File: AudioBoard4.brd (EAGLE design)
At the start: 165.2 x 136.7 mm, 294 parts, among them IC1 TL084D, IC10 TL084D, IC11 TL074D, IC13 SSM2164P, IC14 TL071D, IC15 TL084D, IC16 TL071D, IC17 TL084D, IC18 SSM2164P, IC19 TL071D, IC2 TL074D, IC20 TL084D, IC21 TL071D, IC22 TL084D, IC23 TL072D, IC24 LT1054, IC25 7905, IC26 7805, IC4 TL084D, IC5 TL074D, IC7 TL084D, IC8 TL074D

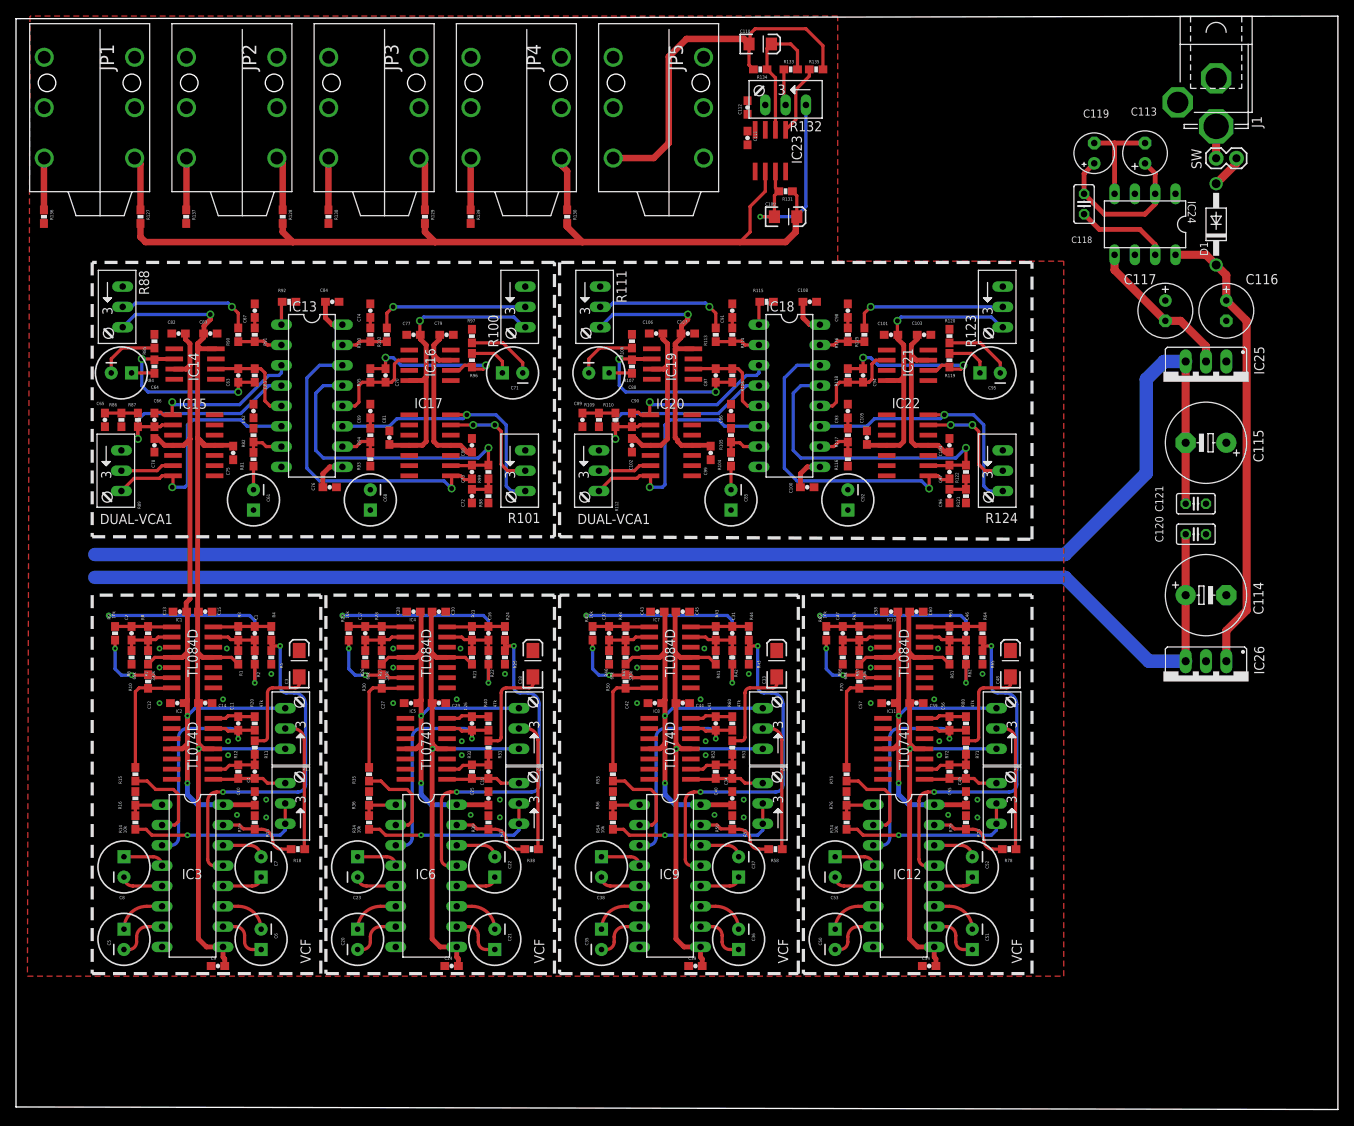
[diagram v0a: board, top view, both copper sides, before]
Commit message: Update eagle files to contain powerdown signal.
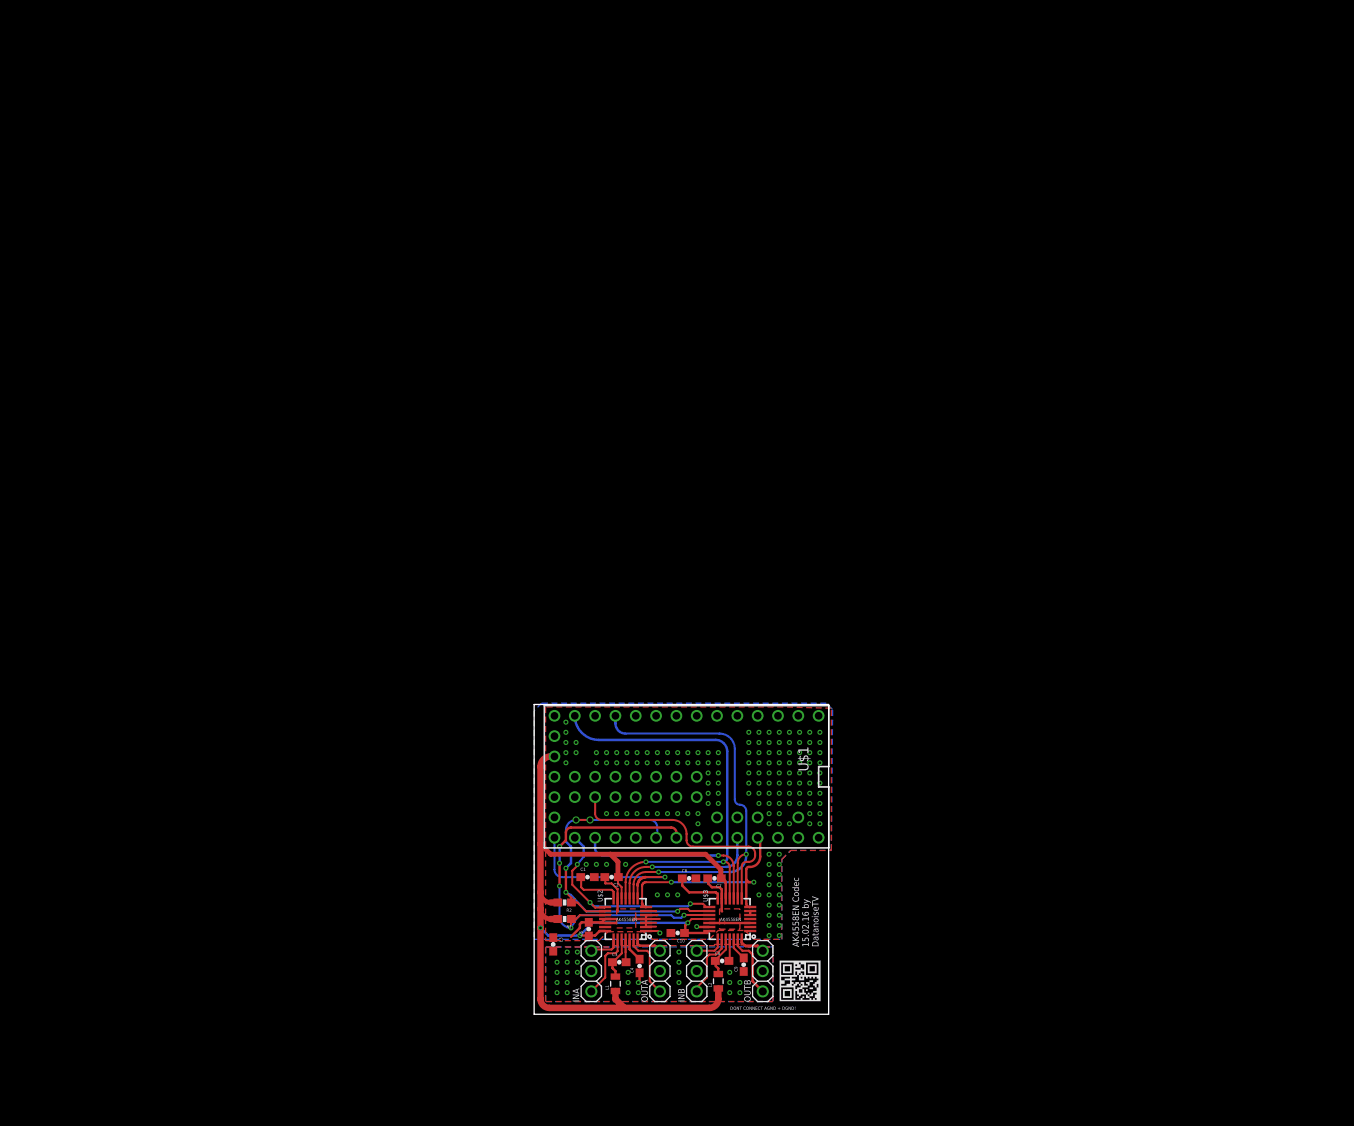
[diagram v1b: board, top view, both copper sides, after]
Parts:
- removed C100, C101, C102, C103, C104, C105, C106, C107, C108, C111, C112, C75, C76, C77, C78, C79, C80, C81, C82, C83, C84, C99: 100n, SparkFun-Capacitors:0603-CAP
- removed C109: 100p, SparkFun-Capacitors:EIA3216
- removed C11, C26, C41, C56: 100pF, SparkFun-Capacitors:0603-CAP
- removed C110: 18p, SparkFun-Capacitors:EIA3216
- removed C113: 100u, rcl:E2,5-6
- removed C114, C115: 220u, rcl:E5-10,5
- removed C116, C117: 100u, rcl:E2,5-7
- removed C118: 10p, rcl:C025-025X050
- removed C119: 10u, rcl:E2,5-5
- removed C12, C13, C14, C15, C24, C25, C27, C28, C29, C30, C39, C40, C42, C43, C44, C45, C54, C55, C57, C58, C59, C60: 100nF, SparkFun-Capacitors:0603-CAP
- removed C120, C121: 100n, rcl:C025-025X050
- removed C16, C17, C31, C32, C46, C47: 22nF, SparkFun-Capacitors:0603-CAP
- removed C18, C33, C48: (no value), SparkFun-Capacitors:EIA3216-KIT
- removed C19, C34, C49: 1.5nF, SparkFun-Capacitors:0603-CAP
- removed C20, C21, C22, C35, C36, C37, C50, C51, C52: 10n, SparkFun-Passives:CPOL-RADIAL-100UF-25V
- removed C23, C38, C53: 820p, SparkFun-Capacitors:CPOL-RADIAL-100UF-25V
- removed C61, C68, C85, C92: 1uF, SparkFun-Capacitors:CPOL-RADIAL-100UF-25V
- removed C62, C67, C69, C74, C86, C91, C93, C98: 560p, SparkFun-Capacitors:0603-CAP
- removed C63, C66, C70, C73, C87, C90, C94, C97: 100p, SparkFun-Capacitors:0603-CAP
- removed C64, C71, C88, C95: 10uF, SparkFun-Capacitors:CPOL-RADIAL-100UF-25V
- removed C65, C72, C89, C96: 33nF, SparkFun-Capacitors:0603-CAP
- removed D1: 1N4001, diode:DO41-10
- removed IC1, IC10, IC15, IC17, IC20, IC22, IC4, IC7: TL084D, linear:SO14
- removed IC11, IC2, IC5, IC8: TL074D, linear:SO14
- removed IC12, IC3, IC6, IC9: (no value), ic-package:DIL16
- removed IC13, IC18: SSM2164P, ssm2164:DIL16
- removed IC14, IC16, IC19, IC21: TL071D, linear:SO08
- removed IC23: TL072D, linear:SO08
- removed IC24: LT1054, ic-package:DIL08
- removed IC25: 7905, v-reg:79XXS
- removed IC26: 7805, v-reg:78XXS
- removed J1: (no value), con-jack2:SPC4078_BIG_HOLES
- removed JP1, JP2, JP3, JP4, JP5: AUDIO-JACK4-.25-HORIZ-TRS, SparkFun-Connectors:AUDIO-JACK-.25-INCH-HORIZ-PTH
- removed R10, R108, R109, R110, R12, R120, R121, R122, R14, R24, R29, R30, R32, R34, R4, R44, R49, R50, R52, R54, R64, R69, R70, R72, R74, R85, R86, R87, R9, R97, R98, R99: 10k, SparkFun-Passives:0603-RES
- removed R100, R111, R123, R88: 100k, pot:RJ9W
- removed R101, R112, R124, R89: 50k, pot:RJ9W
- removed R102, R113, R125, R133, R134, R21, R41, R61, R90: 100k, SparkFun-Passives:0603-RES
- removed R103, R105, R114, R117, R126, R135, R136, R137, R138, R139, R82, R91, R94: 470, SparkFun-Passives:0603-RES
- removed R104, R116, R22, R42, R62, R81, R93: 33k, SparkFun-Passives:0603-RES
- removed R106, R118, R20, R40, R60, R80, R83, R95: 47k, SparkFun-Passives:0603-RES
- removed R107, R119, R15, R35, R55, R75, R84, R96: 150, SparkFun-Passives:0603-RES
- removed R11, R23, R28, R3, R31, R43, R48, R51, R63, R68, R71, R8: 22k, SparkFun-Passives:0603-RES
- removed R115, R92: 4.7k, SparkFun-Passives:0603-RES
- removed R127, R128, R129, R130: 10K, SparkFun-Passives:0603-RES
- removed R13, R33, R53, R73: INPUT_LVL, pot:RJ9W
- removed R131: RGAIN, SparkFun-Passives:0603-RES
- removed R132: 100K, pot:RJ9W
- removed R16, R19, R36, R39, R56, R59, R76, R79: 220, SparkFun-Passives:0603-RES
- removed R17, R37, R57, R77: OFFS_ADJ, pot:RJ9W
- removed R18, R38, R58, R78: 390k, SparkFun-Passives:0603-RES
- removed R25, R45, R5, R65: 1k, SparkFun-Passives:0603-RES
- removed R26, R46, R6, R66: 68k, SparkFun-Passives:0603-RES
- removed R27, R47, R67, R7: 330k, SparkFun-Passives:0603-RES
- removed SW: (no value), SparkFun:1X02
- added INA, INB, OUTA, OUTB: (no value), adafruit:1X03
- added L1, L2: 10uH, SparkFun-Passives:0805
- added L3: 10uH, SparkFun-Passives:0603
- added U$1: TEENSY_3.0_ALL_PINS_AND_PADS, Teensy_3_Series_Board_v1.0:TEENSY_3.0_ALLPINS
- added U$2, U$3: AK4558EN, AK4558:QFN-28-5MM
- C1, C2: value 22nF -> 100n; device SparkFun-Capacitors:0603-CAP -> SparkFun-Passives:0603-CAP
- C10, C9: value 100nF -> 100n; device SparkFun-Capacitors:0603-CAP -> SparkFun-Passives:0603-CAP
- C3: value (none) -> 100n; device SparkFun-Capacitors:EIA3216-KIT -> SparkFun-Passives:0603-CAP
- C4: value 1.5nF -> 100n; device SparkFun-Capacitors:0603-CAP -> SparkFun-Passives:0603-CAP
- C5, C6, C7: value 10n -> 100n; device SparkFun-Passives:CPOL-RADIAL-100UF-25V -> SparkFun-Passives:0603-CAP
- C8: value 820p -> 100n; device SparkFun-Capacitors:CPOL-RADIAL-100UF-25V -> SparkFun-Passives:0603-CAP
- R1: value 100k -> 1k
- R2: value 33k -> 1k
- moved C8 75.7 mm to (87.6, 18.4), turned to 0 degrees
- moved C2 67.3 mm to (73.8, 28.9), turned to 180 degrees
- moved C9 65.7 mm to (90.3, 17.9), turned to 90 degrees
- moved C5 58.1 mm to (71.0, 22.4)
- moved C7 56.7 mm to (86.7, 28.7), turned to 180 degrees
- moved C10 55.5 mm to (82.1, 21.9), turned to 180 degrees
- moved C3 54.7 mm to (74.8, 18.3), turned to 0 degrees
- moved C6 54.0 mm to (83.5, 28.7), turned to 0 degrees
- moved C4 53.9 mm to (77.3, 17.8), turned to 90 degrees
- moved R1 52.3 mm to (67.9, 23.7), turned to 180 degrees
- moved C1 51.6 mm to (70.8, 28.9), turned to 0 degrees
- moved R2 49.4 mm to (67.9, 25.7), turned to 180 degrees
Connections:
- removed net N$100: C63.2, IC13.5, IC14.2, R83.1
- removed net N$101: C63.1, IC14.6, R83.2, R84.1
- removed net N$102: C64.1, R84.2
- removed net N$103: C65.2, R86.2, R87.1
- removed net N$104: C66.2, IC13.4, IC15.2, R87.2
- removed net N$105: C66.1, IC13.3, IC15.1, IC15.5
- removed net N$106: IC13.2, R90.1, R91.2
- removed net N$107: R88.S, R90.2
- removed net N$108: C67.2, R91.1
- removed net N$109: IC13.6, IC15.7, R89.A
- removed net N$110: IC15.6, R89.S
- removed net N$111: IC13.1, R92.2
- removed net N$112: C68.2, R93.1
- removed net N$113: IC13.10, R93.2, R94.2
- removed net N$114: C69.2, R94.1
- removed net N$115: C70.2, IC13.12, IC16.2, R95.1
- removed net N$116: C70.1, IC16.6, R95.2, R96.1
- removed net N$117: C71.1, R96.2
- removed net N$118: IC13.11, IC17.7, R101.A
- removed net N$119: C72.2, R98.2, R99.1
- removed net N$120: C73.2, IC13.13, IC17.2, R99.2
- removed net N$121: C73.1, IC13.14, IC17.1, IC17.5
- removed net N$122: IC13.15, R102.1, R103.2
- removed net N$123: R100.S, R102.2
- removed net N$124: C74.2, R103.1
- removed net N$125: IC17.6, R101.S
- removed net N$126: C85.2, R104.1
- removed net N$127: IC18.7, R104.2, R105.2
- removed net N$128: C86.2, R105.1
- removed net N$129: C87.2, IC18.5, IC19.2, R106.1
- removed net N$130: C87.1, IC19.6, R106.2, R107.1
- removed net N$131: C88.1, R107.2
- removed net N$132: C89.2, R109.2, R110.1
- removed net N$133: C90.2, IC18.4, IC20.2, R110.2
- removed net N$134: C90.1, IC18.3, IC20.1, IC20.5
- removed net N$135: IC18.2, R113.1, R114.2
- removed net N$136: R111.S, R113.2
- removed net N$137: C91.2, R114.1
- removed net N$138: IC18.6, IC20.7, R112.A
- removed net N$139: IC20.6, R112.S
- removed net N$140: IC18.1, R115.2
- removed net N$141: C92.2, R116.1
- removed net N$142: IC18.10, R116.2, R117.2
- removed net N$143: C93.2, R117.1
- removed net N$144: C94.2, IC18.12, IC21.2, R118.1
- removed net N$145: C94.1, IC21.6, R118.2, R119.1
- removed net N$146: C95.1, R119.2
- removed net N$147: IC18.11, IC22.7, R124.A
- removed net N$148: C96.2, R121.2, R122.1
- removed net N$149: C97.2, IC18.13, IC22.2, R122.2
- removed net N$150: C97.1, IC18.14, IC22.1, IC22.5
- removed net N$151: IC18.15, R125.1, R126.2
- removed net N$152: R123.S, R125.2
- removed net N$153: C98.2, R126.1
- removed net N$154: IC22.6, R124.S
- removed net N$155: C109.A, IC23.6, R127.2, R128.2, R129.2, R130.2, R131.1
- removed net N$156: C109.C, IC23.7, R131.2, R132.E
- removed net N$157: R132.S, R133.1
- removed net N$158: C110.A, IC23.2, R133.2, R134.1
- removed net N$159: C110.C, JP5.TIP, R134.2, R135.2
- removed net N$160: IC23.1, R135.1
- removed net N$161: JP1.TIP-NORM, R127.1
- removed net N$162: JP2.TIP-NORM, R128.1
- removed net N$163: JP3.TIP-NORM, R129.1
- removed net N$164: JP4.TIP-NORM, R130.1
- removed net N$165: JP1.TIP, R136.1
- removed net N$166: JP2.TIP, R137.1
- removed net N$167: JP3.TIP, R138.1
- removed net N$168: JP4.TIP, R139.1
- removed net N$169: J1.3, SW.1
- removed net N$17: C7.1, IC3.12
- removed net N$170: C116.+, D1.C, IC24.8, IC26.IN
- removed net N$171: C113.+, C118.1, C119.+, IC24.2
- removed net N$172: C113.-, C119.-, IC24.4
- removed net N$173: C117.-, IC24.5, IC25.IN
- removed net N$174: D1.A, SW.2
- removed net N$175: C118.2, IC24.7
- removed net N$18: C5.1, IC3.6
- removed net N$19: C8.1, IC3.4
- removed net N$20: C6.2, IC3.11
- removed net N$21: C7.2, IC3.14
- removed net N$22: C16.1, IC4.13, R21.2, R22.2, R23.1
- removed net N$23: R17.S, R18.2
- removed net N$24: IC3.15, R18.1, R19.2
- removed net N$25: C11.1, IC2.13, IC3.3, R20.1
- removed net N$26: C16.2, IC4.14, R23.2, R24.1
- removed net N$27: IC6.13, R24.2, R25.2
- removed net N$28: C17.1, IC4.2, R26.2, R27.2, R28.1
- removed net N$29: C17.2, IC4.1, R28.2, R29.1
- removed net N$3: IC3.13, R4.2, R5.2
- removed net N$30: IC4.6, R29.2, R30.1
- removed net N$31: IC4.7, R30.2, R35.1
- removed net N$32: C19.1, IC5.9, R31.1, R32.2
- removed net N$33: C18.C, R31.2
- removed net N$34: C19.2, IC5.8, R32.1, R33.A
- removed net N$35: R33.E, R33.S, R34.1
- removed net N$36: IC6.2, R35.2
- removed net N$37: IC6.1, R34.2, R36.1
- removed net N$38: C20.2, IC6.7
- removed net N$39: C23.2, IC6.5
- removed net N$40: C21.1, IC6.10
- removed net N$41: C22.1, IC6.12
- removed net N$42: C20.1, IC6.6
- removed net N$43: C23.1, IC6.4
- removed net N$44: C21.2, IC6.11
- removed net N$45: C22.2, IC6.14
- removed net N$46: R37.S, R38.2
- removed net N$47: IC6.15, R38.1, R39.2
- removed net N$48: C26.1, IC5.13, IC6.3, R40.1
- removed net N$49: C31.1, IC7.13, R41.2, R42.2, R43.1
- removed net N$5: C2.2, IC1.1, R8.2, R9.1
- removed net N$50: C31.2, IC7.14, R43.2, R44.1
- removed net N$51: IC9.13, R44.2, R45.2
- removed net N$52: C32.1, IC7.2, R46.2, R47.2, R48.1
- removed net N$53: C32.2, IC7.1, R48.2, R49.1
- removed net N$54: IC7.6, R49.2, R50.1
- removed net N$55: IC7.7, R50.2, R55.1
- removed net N$56: C34.1, IC8.9, R51.1, R52.2
- removed net N$57: C33.C, R51.2
- removed net N$58: C34.2, IC8.8, R52.1, R53.A
- removed net N$59: R53.E, R53.S, R54.1
- removed net N$60: IC9.2, R55.2
- removed net N$61: IC9.1, R54.2, R56.1
- removed net N$62: C35.2, IC9.7
- removed net N$63: C38.2, IC9.5
- removed net N$64: C36.1, IC9.10
- removed net N$65: C37.1, IC9.12
- removed net N$66: C35.1, IC9.6
- removed net N$67: C38.1, IC9.4
- removed net N$68: C36.2, IC9.11
- removed net N$69: C37.2, IC9.14
- removed net N$70: R57.S, R58.2
- removed net N$71: IC9.15, R58.1, R59.2
- removed net N$72: C41.1, IC8.13, IC9.3, R60.1
- removed net N$73: C46.1, IC10.13, R61.2, R62.2, R63.1
- removed net N$74: C46.2, IC10.14, R63.2, R64.1
- removed net N$75: IC12.13, R64.2, R65.2
- removed net N$76: C47.1, IC10.2, R66.2, R67.2, R68.1
- removed net N$77: C47.2, IC10.1, R68.2, R69.1
- removed net N$78: IC10.6, R69.2, R70.1
- removed net N$79: IC10.7, R70.2, R75.1
- removed net N$80: C49.1, IC11.9, R71.1, R72.2
- removed net N$81: C48.C, R71.2
- removed net N$82: C49.2, IC11.8, R72.1, R73.A
- removed net N$83: R73.E, R73.S, R74.1
- removed net N$84: IC12.2, R75.2
- removed net N$85: IC12.1, R74.2, R76.1
- removed net N$86: C50.2, IC12.7
- removed net N$87: C53.2, IC12.5
- removed net N$88: C51.1, IC12.10
- removed net N$89: C52.1, IC12.12
- removed net N$90: C50.1, IC12.6
- removed net N$91: C53.1, IC12.4
- removed net N$92: C51.2, IC12.11
- removed net N$93: C52.2, IC12.14
- removed net N$94: R77.S, R78.2
- removed net N$95: IC12.15, R78.1, R79.2
- removed net N$96: C56.1, IC11.13, IC12.3, R80.1
- removed net N$97: C61.2, R81.1
- removed net N$98: IC13.7, R81.2, R82.2
- removed net N$99: C62.2, R82.1
- removed net VCAA_AMP_IN1: R109.1, R86.1
- removed net VCAA_OUT1: C64.2, C88.2, R108.2, R85.2
- removed net VCAA_OUT2: R136.2
- removed net VCAA_OUT3: R138.2
- removed net VCAB_AMP_IN1: R121.1, R98.1
- removed net VCAB_OUT1: C71.2, C95.2, R120.2, R97.2
- removed net VCAB_OUT2: R137.2
- removed net VCAB_OUT3: R139.2
- removed net VCC: C10.2, C102.1, C103.1, C104.1, C106.1, C108.1, C111.1, C114.+, C12.2, C120.1, C13.2, C25.2, C27.2, C28.2, C40.2, C42.2, C43.2, C55.2, C57.2, C58.2, C78.1, C79.1, C80.1, C82.1, C84.1, IC1.4, IC10.4, IC11.4, IC12.16, IC13.16, IC14.7, IC15.4, IC16.7, IC17.4, IC18.16, IC19.7, IC2.4, IC20.4, IC21.7, IC22.4, IC23.8, IC26.OUT, IC3.16, IC4.4, IC5.4, IC6.16, IC7.4, IC8.4, IC9.16, R115.1, R17.A, R27.1, R37.A, R47.1, R57.A, R67.1, R7.1, R77.A, R92.1
- removed net VCF_AUDIO1: C3.A
- removed net VCF_AUDIO2: C18.A
- removed net VCF_AUDIO3: C33.A
- removed net VCF_AUDIO4: C48.A
- removed net VCF_CUTOFF1: R2.1
- removed net VCF_CUTOFF2: R22.1
- removed net VCF_CUTOFF3: R42.1
- removed net VCF_CUTOFF4: R62.1
- removed net VCF_OUT1: C11.2, C61.1, IC2.14, R20.2
- removed net VCF_OUT2: C26.2, C68.1, IC5.14, R40.2
- removed net VCF_OUT3: C41.2, C85.1, IC8.14, R60.2
- removed net VCF_OUT4: C56.2, C92.1, IC11.14, R80.2
- removed net VCF_RES1: R6.1
- removed net VCF_RES2: R26.1
- removed net VCF_RES3: R46.1
- removed net VCF_RES4: R66.1
- removed net VEE: C100.2, C101.1, C105.1, C107.1, C112.1, C115.-, C121.2, C14.1, C15.1, C24.2, C29.1, C30.1, C39.2, C44.1, C45.1, C54.2, C59.1, C60.1, C75.2, C76.2, C77.1, C81.1, C83.1, C9.2, C99.2, IC1.11, IC10.11, IC11.11, IC12.9, IC13.9, IC14.4, IC15.11, IC16.4, IC17.11, IC18.9, IC19.4, IC2.11, IC20.11, IC21.4, IC22.11, IC23.4, IC25.OUT, IC3.9, IC4.11, IC5.11, IC6.9, IC7.11, IC8.11, IC9.9, R1.1, R100.A, R111.A, R123.A, R17.E, R21.1, R37.E, R41.1, R57.E, R61.1, R77.E, R88.A
- new net AGND: U$1.AGND
- new net AREF: U$1.AREF
- new net BCLK: U$1.9, U$2.P$9, U$3.P$9
- new net GNDA: C3.2, C4.1, C8.2, C9.1, INA.2, INB.2, L3.2, OUTA.2, OUTB.2, U$2.P$25, U$3.P$25
- new net LRCLK: U$1.23/A9, U$2.P$7, U$3.P$7
- new net MCLK: U$1.11, U$2.P$11, U$3.P$11
- new net PDN: U$1.14/A0, U$2.P$15, U$3.P$15
- new net RX: U$1.13, U$2.P$8
- new net RX1: U$1.30, U$3.P$8
- new net SCL: R1.1, U$1.19/A5, U$2.P$17, U$3.P$17
- new net SDA: R2.1, U$1.18/A4, U$2.P$16, U$3.P$16
- new net TX: U$1.22/A8, U$2.P$10
- new net TX1: U$1.15/A1, U$3.P$10
- new net VBAT: U$1.VBAT
- new net VDD: C10.1, C2.1, C5.1, C7.1, L1.1, L2.1, R1.2, R2.2, U$1.3.3V, U$1.3.3V1, U$1.3.3V2, U$2.P$12, U$2.P$21, U$3.P$12, U$3.P$18, U$3.P$21
- new net VIN: U$1.VIN
- new net VUSB: U$1.VUSB
- net GND: now also C1.2, C10.2, C2.2, C5.2, C6.2, C7.2, L3.1, U$1.GND, U$1.GND1, U$1.GND2, U$2.P$1, U$2.P$13, U$2.P$18, U$2.P$19, U$2.P$2, U$2.P$20, U$2.P$3, U$2.P$4, U$2.P$5, U$2.P$6, U$3.P$1, U$3.P$13, U$3.P$19, U$3.P$2, U$3.P$20, U$3.P$3, U$3.P$4, U$3.P$5, U$3.P$6; no longer C10.1, C100.1, C101.2, C102.2, C103.2, C104.2, C105.2, C106.2, C107.2, C108.2, C111.2, C112.2, C114.-, C115.+, C116.-, C117.+, C12.1, C120.2, C121.1, C13.1, C14.2, C15.2, C24.1, C25.1, C27.1, C28.1, C29.2, C30.2, C39.1, C40.1, C42.1, C43.1, C44.2, C45.2, C54.1, C55.1, C57.1, C58.1, C59.2, C60.2, C62.1, C65.1, C67.1, C69.1, C72.1, C74.1, C75.1, C76.1, C77.2, C78.2, C79.2, C80.2, C81.2, C82.2, C83.2, C84.2, C86.1, C89.1, C9.1, C91.1, C93.1, C96.1, C98.1, C99.1, IC1.12, IC1.3, IC1.5, IC10.12, IC10.3, IC10.5, IC11.10, IC11.12, IC12.8, IC13.8, IC14.3, IC16.3, IC18.8, IC19.3, IC2.10, IC2.12, IC21.3, IC23.3, IC23.5, IC24.3, IC25.GND, IC26.GND, IC3.8, IC4.12, IC4.3, IC4.5, IC5.10, IC5.12, IC6.8, IC7.12, IC7.3, IC7.5, IC8.10, IC8.12, IC9.8, J1.1, JP1.SLEEVE, JP1.SLEEVE-NORM, JP2.SLEEVE, JP2.SLEEVE-NORM, JP3.SLEEVE, JP3.SLEEVE-NORM, JP4.SLEEVE, JP4.SLEEVE-NORM, JP5.SLEEVE, JP5.SLEEVE-NORM, R100.E, R101.E, R108.1, R111.E, R112.E, R120.1, R123.E, R124.E, R132.A, R16.2, R19.1, R25.1, R36.2, R39.1, R45.1, R5.1, R56.2, R59.1, R65.1, R76.2, R79.1, R85.1, R88.E, R89.E, R97.1
- net N$1: now also U$2.P$14; no longer IC1.13, R1.2, R2.2, R3.1
- net N$10: now also C6.1, U$3.P$14; no longer C4.2, IC2.8, R12.1, R13.A
- net N$11: now also C8.1, L2.2, U$3.P$24; no longer R13.E, R13.S, R14.1
- net N$12: now also C9.2, U$3.P$26; no longer IC3.2, R15.2
- net N$13: now also INB.1, U$3.P$22; no longer IC3.1, R14.2, R16.1
- net N$14: now also INB.3, U$3.P$23; no longer C5.2, IC3.7
- net N$15: now also OUTB.1, U$3.P$27; no longer C8.2, IC3.5
- net N$16: now also OUTB.3, U$3.P$28; no longer C6.1, IC3.10
- net N$2: now also C3.1, L1.2, U$2.P$24; no longer C1.2, IC1.14, R3.2, R4.1
- net N$4: now also C4.2, U$2.P$26; no longer C2.1, IC1.2, R6.2, R7.2, R8.1
- net N$6: now also INA.1, U$2.P$22; no longer IC1.6, R10.1, R9.2
- net N$7: now also INA.3, U$2.P$23; no longer IC1.7, R10.2, R15.1
- net N$8: now also OUTA.1, U$2.P$27; no longer C4.1, IC2.9, R11.1, R12.2
- net N$9: now also OUTA.3, U$2.P$28; no longer C3.C, R11.2
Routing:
- net VEE: track 616.7 -> 0.00 mm, vias 8 -> 0
- net VCC: track 482.7 -> 0.00 mm, vias 8 -> 0
- net VDD: track 0.00 -> 129.0 mm, vias 0 -> 3
- net N$155: track 108.7 -> 0.00 mm
- net N$170: track 57.8 -> 0.00 mm
- net MCLK: track 0.00 -> 55.2 mm, vias 0 -> 2
- net BCLK: track 0.00 -> 54.5 mm, vias 0 -> 2
- net SCL: track 0.00 -> 52.0 mm, vias 0 -> 5
- net N$159: track 48.8 -> 0.00 mm
- net SDA: track 0.00 -> 47.5 mm, vias 0 -> 5
- net N$3: track 44.3 -> 0.00 mm, vias 2 -> 0
- net N$51: track 44.3 -> 0.00 mm, vias 2 -> 0
- net N$27: track 44.3 -> 0.00 mm, vias 2 -> 0
- net N$75: track 44.3 -> 0.00 mm, vias 2 -> 0
- net N$149: track 40.3 -> 0.00 mm, vias 1 -> 0
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- added copper zone on layer 16, net GND
- added copper zone on layer 1, net GNDA
- added copper zone on layer 16, net GNDA
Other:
- board size 165.2 x 136.7 mm -> 36.8 x 38.7 mm
- board text added: "AK4558EN Codec 15.02.16 by DatanoiseTV"
- board text added: "DONT CONNECT AGND + DGND!"
- board text removed: "DUAL-VCA1"
- board text removed: "VCF"
